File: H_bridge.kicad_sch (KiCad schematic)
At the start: 47 parts, among them J1 Conn_01x02_Female, J18 Conn_01x03_Female, SW7 SW_SPST, T3 AOD4132, T4 AOD4132, T5 AOD4132, T6 AOD4132, U1 IR2104, U2 IR2104, U35 AP331A

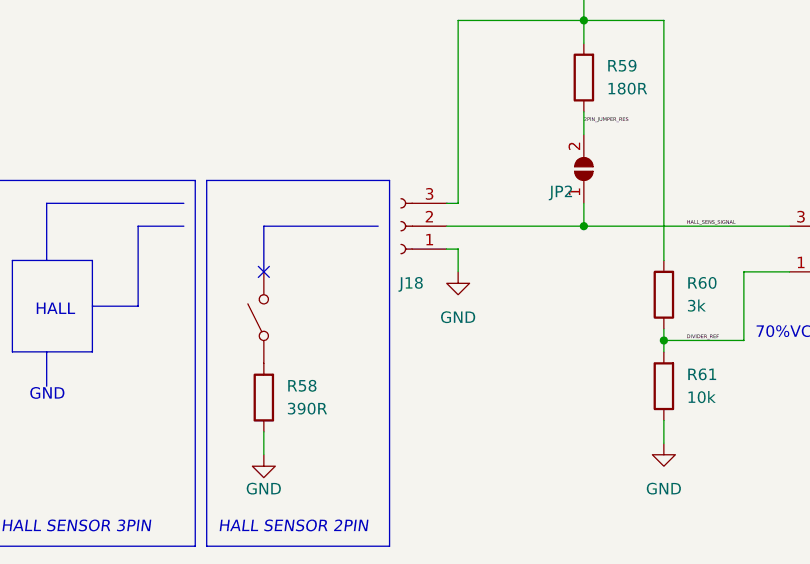
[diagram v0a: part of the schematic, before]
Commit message: finished H-bridge layouts and replicate
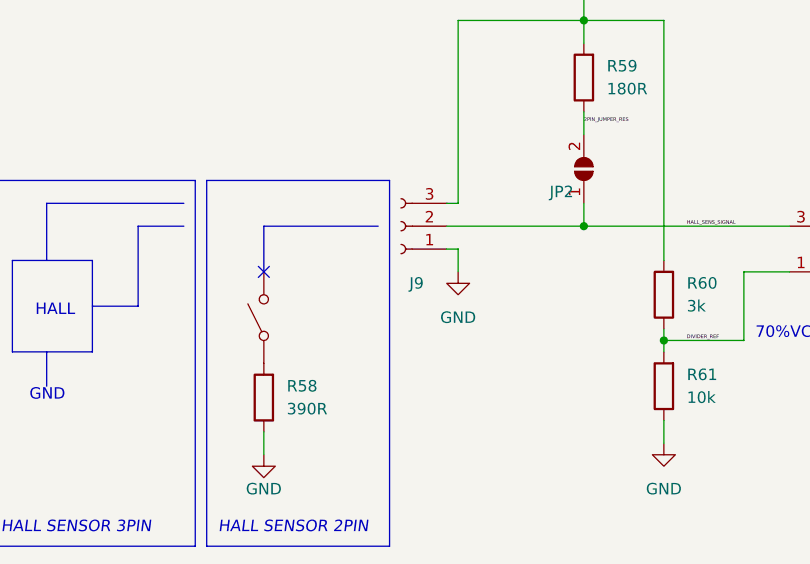
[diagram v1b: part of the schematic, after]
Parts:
- renumbered J18 to J9, SW7 to SW1
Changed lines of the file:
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@@
   (symbol (lib_id "Connector:Conn_01x03_Female") (at 66.04 154.94 180) (unit 1)
     (in_bom yes) (on_board yes)
-    (property "Reference" "J18" (id 0) (at 68.58 161.29 0)
+    (property "Reference" "J9" (id 0) (at 68.58 161.29 0)
       (effects (font (size 1.27 1.27)) (justify left))
     )
@@
   (symbol (lib_id "Switch:SW_SPST") (at 50.8 165.1 90) (unit 1)
     (in_bom no) (on_board no) (fields_autoplaced)
-    (property "Reference" "SW7" (id 0) (at 52.07 163.8299 90)
+    (property "Reference" "SW1" (id 0) (at 52.07 163.8299 90)
       (effects (font (size 1.27 1.27)) (justify right) hide)
     )

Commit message: v2.1 finished
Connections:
- net MOTOR_VOLTAGE: no longer J9.3 (Pin_3), R59.2, R60.2, U35.5 (V+)
- new net SENSE_VOLTAGE: J9.3 (Pin_3), R59.2, R60.2, U35.5 (V+)
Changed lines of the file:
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@@
   (junction (at 177.8 77.47) (diameter 0) (color 0 0 0 0)
+  )
+  (junction (at 121.92 118.11) (diameter 0) (color 0 0 0 0)
   )
   (no_connect (at 50.8 160.02))
@@
     (stroke (width 0) (type default) (color 0 0 0 0))
   )
-  (wire (pts (xy 86.36 121.92) (xy 86.36 132.08))
+  (wire (pts (xy 86.36 118.11) (xy 86.36 132.08))
     (stroke (width 0) (type default) (color 0 0 0 0))
   )
@@
     (stroke (width 0) (type default) (color 255 82 172 1))
   )
+  (wire (pts (xy 154.94 118.11) (xy 121.92 118.11))
+    (stroke (width 0) (type default) (color 0 0 0 0))
+  )
   (wire (pts (xy 59.69 69.85) (xy 74.93 69.85))
     (stroke (width 0) (type default) (color 0 0 0 0))
@@
     (stroke (width 0) (type default) (color 0 0 0 0))
   )
-  (wire (pts (xy 154.94 146.05) (xy 154.94 151.13))
+  (wire (pts (xy 154.94 118.11) (xy 154.94 151.13))
     (stroke (width 0) (type default) (color 0 0 0 0))
   )
@@
     (stroke (width 0) (type default) (color 0 0 0 0))
   )
+  (wire (pts (xy 121.92 118.11) (xy 86.36 118.11))
+    (stroke (width 0) (type default) (color 0 0 0 0))
+  )
   (wire (pts (xy 172.72 60.96) (xy 173.99 60.96))
     (stroke (width 0) (type default) (color 0 0 0 0))
@@
   )
   (polyline (pts (xy 50.8 160.02) (xy 50.8 154.94))
+    (stroke (width 0) (type default) (color 0 0 0 0))
+  )
+  (wire (pts (xy 121.92 115.57) (xy 121.92 118.11))
     (stroke (width 0) (type default) (color 0 0 0 0))
   )
@@
     (effects (font (size 1.27 1.27)) (justify left bottom))
   )
-  (label "MOTOR_VOLTAGE" (at 154.94 146.05 90)
-    (effects (font (size 1.27 1.27)) (justify left bottom))
-  )
   (label "HO_CCW" (at 198.12 64.77 0)
     (effects (font (size 0.4 0.4)) (justify left bottom))
@@
   (label "BOOTSTRAP_CCW" (at 195.58 62.23 90)
     (effects (font (size 0.4 0.4)) (justify left bottom))
-  )
-  (label "MOTOR_VOLTAGE" (at 86.36 121.92 90)
-    (effects (font (size 1.27 1.27)) (justify left bottom))
   )
   (label "HALL_SENS_SIGNAL" (at 97.79 154.94 0)
@@
     (effects (font (size 1.27 1.27)) (justify left))
   )
+  (hierarchical_label "SENSE_VOLTAGE" (shape input) (at 121.92 115.57 90)
+    (effects (font (size 1.27 1.27)) (justify left))
+  )

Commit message: changed power loss detection schematic, changed tvs diodes on other type, added two more caps on 3v3 line, change indicator leds resistors
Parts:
- added TP?: TestPoint, TestPoint:TestPoint_THTPad_1.0x1.0mm_Drill0.5mm, symbol Connector:TestPoint
- C3, C5: value 100n_50V -> 100n 50V
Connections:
- net HALL_OUT: now also TP?.1
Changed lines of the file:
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@@
   (junction (at 144.78 44.45) (diameter 0) (color 0 0 0 0)
+  )
+  (junction (at 130.81 157.48) (diameter 0) (color 0 0 0 0)
   )
   (junction (at 123.19 90.17) (diameter 0) (color 0 0 0 0)
@@
     (stroke (width 0) (type default) (color 0 0 0 0))
   )
+  (wire (pts (xy 130.81 157.48) (xy 130.81 162.56))
+    (stroke (width 0) (type default) (color 0 0 0 0))
+  )
   (wire (pts (xy 154.94 118.11) (xy 154.94 151.13))
     (stroke (width 0) (type default) (color 0 0 0 0))
@@
     (stroke (width 0) (type default) (color 0 0 0 0))
   )
+  (wire (pts (xy 130.81 157.48) (xy 133.35 157.48))
+    (stroke (width 0) (type default) (color 0 0 0 0))
+  )
   (wire (pts (xy 123.19 82.55) (xy 123.19 90.17))
     (stroke (width 0) (type default) (color 0 0 0 0))
@@
     (stroke (width 0) (type default) (color 0 0 0 0))
   )
-  (wire (pts (xy 128.27 157.48) (xy 133.35 157.48))
+  (wire (pts (xy 128.27 157.48) (xy 130.81 157.48))
     (stroke (width 0) (type default) (color 0 0 0 0))
   )
@@
     (pin "2")
   )
+  (symbol (lib_id "Connector:TestPoint") (at 130.81 162.56 180) (unit 1)
+    (in_bom yes) (on_board yes)
+    (property "Reference" "TP?" (id 0) (at 129.54 167.64 0)
+      (effects (font (size 1.27 1.27)) (justify right))
+    )
+    (property "Value" "TestPoint" (id 1) (at 133.35 167.1319 0)
+      (effects (font (size 1.27 1.27)) (justify right) hide)
+    )
+    (property "Footprint" "TestPoint:TestPoint_THTPad_1.0x1.0mm_Drill0.5mm" (id 2) (at 125.73 162.56 0)
+      (effects (font (size 1.27 1.27)) hide)
+    )
+    (property "Datasheet" "~" (id 3) (at 125.73 162.56 0)
+      (effects (font (size 1.27 1.27)) hide)
+    )
+    (pin "1")
+  )
   (symbol (lib_id "Connector:TestPoint") (at 187.96 78.74 180) (unit 1)
     (in_bom yes) (on_board yes)
@@
   (symbol (lib_id "Diode:1.5KExxCA") (at 111.76 83.82 90) (unit 1)
     (in_bom yes) (on_board yes)
-    (property "Reference" "D67" (id 0) (at 113.03 87.63 90)
+    (property "Reference" "D67" (id 0) (at 115.57 82.55 0)
       (effects (font (size 1.27 1.27)) (justify right))
     )
@@
       (effects (font (size 1.27 1.27)) (justify left))
     )
-    (property "Value" "100n_50V" (id 1) (at 186.69 57.15 90)
+    (property "Value" "100n 50V" (id 1) (at 186.69 57.15 90)
       (effects (font (size 1.27 1.27)) (justify left))
     )
@@
       (effects (font (size 1.27 1.27)) (justify left))
     )
-    (property "Value" "100n_50V" (id 1) (at 97.79 57.15 90)
+    (property "Value" "100n 50V" (id 1) (at 97.79 57.15 90)
       (effects (font (size 1.27 1.27)) (justify left))
     )
@@
   (symbol (lib_id "Diode:1.5KExxCA") (at 177.8 83.82 90) (unit 1)
     (in_bom yes) (on_board yes)
-    (property "Reference" "D69" (id 0) (at 172.72 85.09 90)
+    (property "Reference" "D69" (id 0) (at 174.7079 82.0842 0)
       (effects (font (size 1.27 1.27)) (justify right))
     )
@@
   (symbol (lib_id "Diode:1.5KExxCA") (at 111.76 66.04 90) (unit 1)
     (in_bom yes) (on_board yes)
-    (property "Reference" "D79" (id 0) (at 107.95 66.04 90)
+    (property "Reference" "D79" (id 0) (at 109.22 63.5 0)
       (effects (font (size 1.27 1.27)) (justify right))
     )
@@
   (symbol (lib_id "Diode:1.5KExxCA") (at 177.8 66.04 90) (unit 1)
     (in_bom yes) (on_board yes)
-    (property "Reference" "D68" (id 0) (at 172.72 67.31 90)
-      (effects (font (size 1.27 1.27)) (justify right))
-    )
+    (property "Reference" "D68" (id 0) (at 174.7079 64.2205 0)
+      (effects (font (size 1.27 1.27)) (justify right))
+    )

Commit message: updated footprints on board and sgematics
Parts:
- D12, D13, D14, D15, D16, D17: footprint Diode_SMD:D_SMA_Handsoldering -> Diode_SMD:D_SMC
- D67, D68, D69, D79: footprint Diode_SMD:D_SMA_Handsoldering -> Diode_THT:D_DO-201AE_P15.24mm_Horizontal
- gave numbers to parts that had none: 1
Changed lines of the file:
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@@
   (symbol (lib_id "Connector:TestPoint") (at 130.81 162.56 180) (unit 1)
     (in_bom yes) (on_board yes)
-    (property "Reference" "TP?" (id 0) (at 129.54 167.64 0)
+    (property "Reference" "TP24" (id 0) (at 129.54 167.64 0)
       (effects (font (size 1.27 1.27)) (justify right))
     )
@@
       (effects (font (size 1.27 1.27)) (justify left))
     )
-    (property "Footprint" "Diode_SMD:D_SMA_Handsoldering" (id 2) (at 126.365 78.74 0)
+    (property "Footprint" "Diode_SMD:D_SMC" (id 2) (at 126.365 78.74 0)
       (effects (font (size 1.27 1.27)) hide)
     )
@@
       (effects (font (size 1.27 1.27)) (justify right))
     )
-    (property "Footprint" "Diode_SMD:D_SMA_Handsoldering" (id 2) (at 116.84 83.82 0)
+    (property "Footprint" "Diode_THT:D_DO-201AE_P15.24mm_Horizontal" (id 2) (at 116.84 83.82 0)
       (effects (font (size 1.27 1.27)) hide)
     )
@@
       (effects (font (size 1.27 1.27)) (justify left))
     )
-    (property "Footprint" "Diode_SMD:D_SMA_Handsoldering" (id 2) (at 126.365 60.96 0)
+    (property "Footprint" "Diode_SMD:D_SMC" (id 2) (at 126.365 60.96 0)
       (effects (font (size 1.27 1.27)) hide)
     )
@@
       (effects (font (size 1.27 1.27)) (justify left))
     )
-    (property "Footprint" "Diode_SMD:D_SMA_Handsoldering" (id 2) (at 151.765 78.74 0)
+    (property "Footprint" "Diode_SMD:D_SMC" (id 2) (at 151.765 78.74 0)
       (effects (font (size 1.27 1.27)) hide)
     )
@@
     (property "Reference" "D12" (id 0) (at 87.9475 40.64 0))
     (property "Value" "B330" (id 1) (at 87.9475 43.18 0))
-    (property "Footprint" "Diode_SMD:D_SMA_Handsoldering" (id 2) (at 87.63 42.545 0)
+    (property "Footprint" "Diode_SMD:D_SMC" (id 2) (at 87.63 42.545 0)
       (effects (font (size 1.27 1.27)) hide)
     )
@@
       (effects (font (size 1.27 1.27)) (justify right))
     )
-    (property "Footprint" "Diode_SMD:D_SMA_Handsoldering" (id 2) (at 182.88 83.82 0)
+    (property "Footprint" "Diode_THT:D_DO-201AE_P15.24mm_Horizontal" (id 2) (at 182.88 83.82 0)
       (effects (font (size 1.27 1.27)) hide)
     )
@@
       (effects (font (size 1.27 1.27)) (justify right))
     )
-    (property "Footprint" "Diode_SMD:D_SMA_Handsoldering" (id 2) (at 116.84 66.04 0)
+    (property "Footprint" "Diode_THT:D_DO-201AE_P15.24mm_Horizontal" (id 2) (at 116.84 66.04 0)
       (effects (font (size 1.27 1.27)) hide)
     )
@@
       (effects (font (size 1.27 1.27)) (justify right))
     )
-    (property "Footprint" "Diode_SMD:D_SMA_Handsoldering" (id 2) (at 182.88 66.04 0)
+    (property "Footprint" "Diode_THT:D_DO-201AE_P15.24mm_Horizontal" (id 2) (at 182.88 66.04 0)
       (effects (font (size 1.27 1.27)) hide)
     )
@@
     (property "Reference" "D17" (id 0) (at 201.6125 40.64 0))
     (property "Value" "B330" (id 1) (at 201.6125 43.18 0))
-    (property "Footprint" "Diode_SMD:D_SMA_Handsoldering" (id 2) (at 201.93 51.435 0)
+    (property "Footprint" "Diode_SMD:D_SMC" (id 2) (at 201.93 51.435 0)
       (effects (font (size 1.27 1.27)) hide)
     )
@@
       (effects (font (size 1.27 1.27)) (justify left))
     )
-    (property "Footprint" "Diode_SMD:D_SMA_Handsoldering" (id 2) (at 151.765 60.96 0)
-      (effects (font (size 1.27 1.27)) hide)
-    )
+    (property "Footprint" "Diode_SMD:D_SMC" (id 2) (at 151.765 60.96 0)
+      (effects (font (size 1.27 1.27)) hide)
+    )
